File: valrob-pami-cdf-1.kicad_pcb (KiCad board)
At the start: 4 copper layers, 58 x 50 mm, 138 parts, among them J1 Conn_01x04, J2 USB_C_Receptacle_USB2.0_14P, J3 Conn_01x02, J4 Conn_01x04_Pin, J5 Conn_01x06, M1 Motor_Servo, M2 Stepper_Motor_bipolar, M3 Stepper_Motor_bipolar, Q1 Q_NMOS, Q2 Q_NMOS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

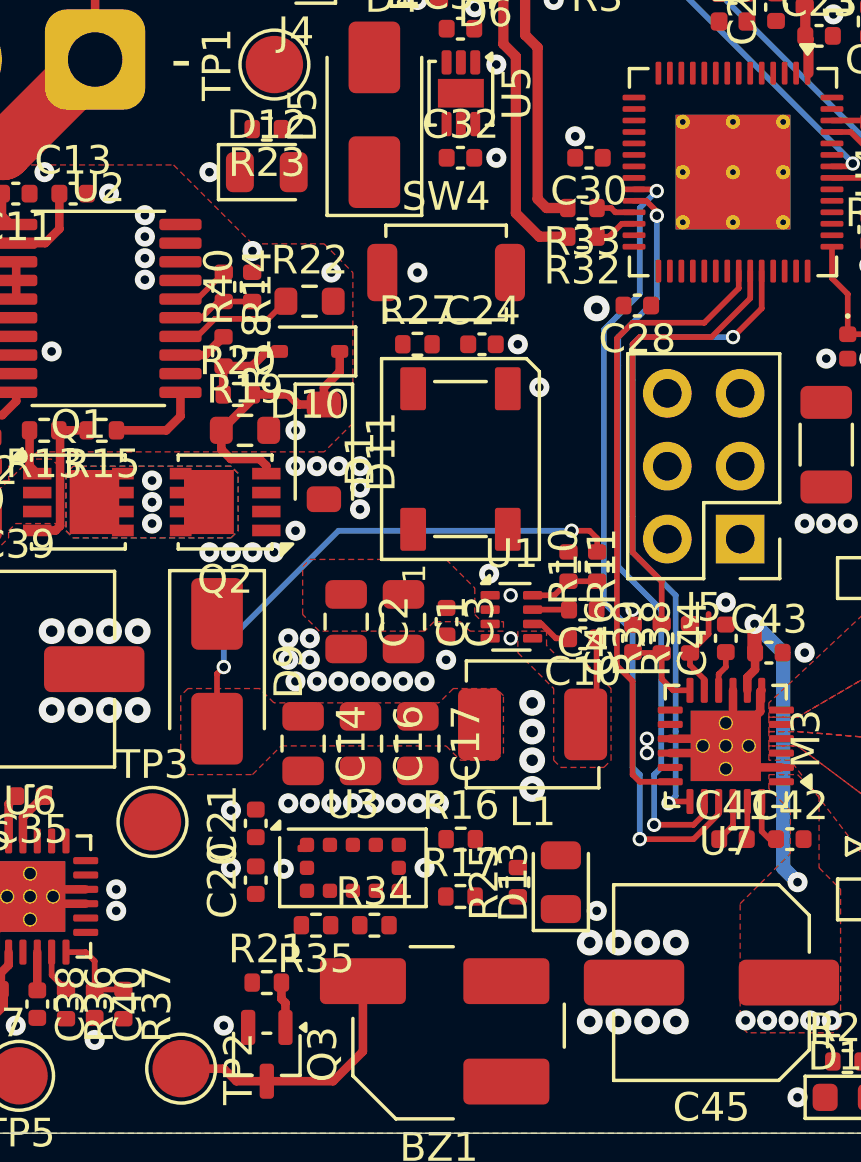
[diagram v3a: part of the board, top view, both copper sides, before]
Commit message: pcb: add buzzer routing
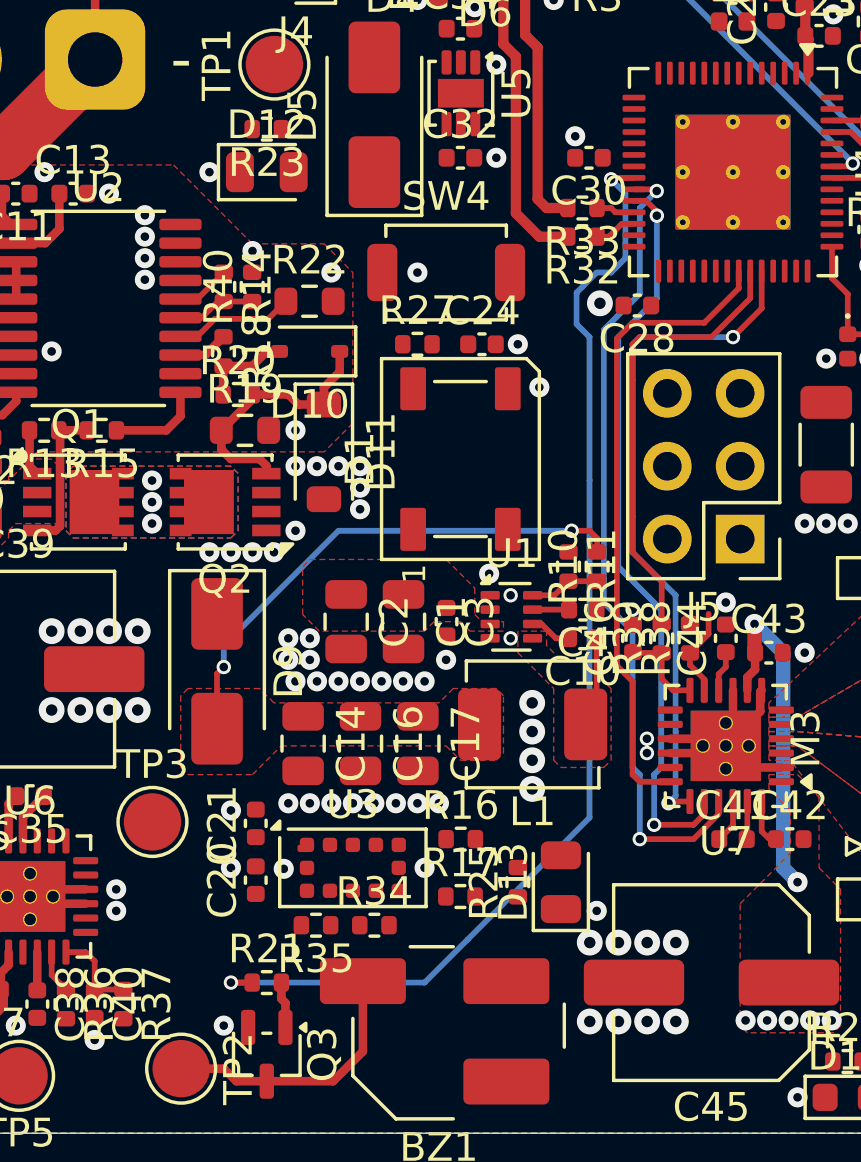
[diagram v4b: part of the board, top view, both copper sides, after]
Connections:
- U4 pad 22: unconnected-(U4-GPIO16/ADC2_CH5/XTAL_32K_N-Pad22) -> /BUZZER
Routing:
- net /BUZZER: track 0.00 -> 40.1 mm, vias 0 -> 2
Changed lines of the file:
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@@
 	(net 110 "unconnected-(U4-SPIQ{slash}GPIO31-Pad34)")
 	(net 111 "/~{SLEEP_2}")
-	(net 112 "unconnected-(U4-GPIO16{slash}ADC2_CH5{slash}XTAL_32K_N-Pad22)")
-	(net 113 "unconnected-(U4-MTDI{slash}JTAG{slash}GPIO41-Pad47)")
-	(net 114 "unconnected-(U6-M1-Pad17)")
-	(net 115 "unconnected-(U6-TOFF-Pad14)")
-	(net 116 "unconnected-(U7-TOFF-Pad14)")
-	(net 117 "unconnected-(U7-M1-Pad17)")
-	(net 118 "unconnected-(D1-DOUT-Pad2)")
-	(net 119 "Net-(J5-Pin_5)")
-	(net 120 "Net-(J5-Pin_4)")
-	(net 121 "Net-(J5-Pin_2)")
-	(net 122 "Net-(J5-Pin_3)")
-	(net 123 "unconnected-(R34-Pad2)")
-	(net 124 "unconnected-(U4-GPIO5{slash}ADC1_CH4-Pad10)")
-	(net 125 "unconnected-(U4-GPIO9{slash}ADC1_CH8-Pad14)")
-	(net 126 "unconnected-(U4-GPIO12{slash}ADC2_CH1-Pad17)")
-	(net 127 "unconnected-(U4-GPIO13{slash}ADC2_CH2-Pad18)")
-	(net 128 "unconnected-(U4-GPIO14{slash}ADC2_CH3-Pad19)")
-	(net 129 "unconnected-(U4-GPIO11{slash}ADC2_CH0-Pad16)")
+	(net 112 "unconnected-(U4-MTDI{slash}JTAG{slash}GPIO41-Pad47)")
+	(net 113 "unconnected-(U6-M1-Pad17)")
+	(net 114 "unconnected-(U6-TOFF-Pad14)")
+	(net 115 "unconnected-(U7-TOFF-Pad14)")
+	(net 116 "unconnected-(U7-M1-Pad17)")
+	(net 117 "unconnected-(D1-DOUT-Pad2)")
+	(net 118 "Net-(J5-Pin_5)")
+	(net 119 "Net-(J5-Pin_4)")
+	(net 120 "Net-(J5-Pin_2)")
+	(net 121 "Net-(J5-Pin_3)")
+	(net 122 "unconnected-(R34-Pad2)")
+	(net 123 "unconnected-(U4-GPIO5{slash}ADC1_CH4-Pad10)")
+	(net 124 "unconnected-(U4-GPIO9{slash}ADC1_CH8-Pad14)")
+	(net 125 "unconnected-(U4-GPIO12{slash}ADC2_CH1-Pad17)")
+	(net 126 "unconnected-(U4-GPIO13{slash}ADC2_CH2-Pad18)")
+	(net 127 "unconnected-(U4-GPIO14{slash}ADC2_CH3-Pad19)")
+	(net 128 "unconnected-(U4-GPIO11{slash}ADC2_CH0-Pad16)")
 	(footprint "GLCS:Texas_RGE0024B_VQFN-24-1EP_4x4mm_P0.5mm_EP2.5x2.5mm_ThermalVias"
 		(layer "F.Cu")
@@
 			(layers "F.Cu" "F.Mask" "F.Paste")
 			(roundrect_rratio 0.25)
-			(net 115 "unconnected-(U6-TOFF-Pad14)")
+			(net 114 "unconnected-(U6-TOFF-Pad14)")
 			(pinfunction "TOFF")
 			(pintype "input+no_connect")
@@
 			(layers "F.Cu" "F.Mask" "F.Paste")
 			(roundrect_rratio 0.25)
-			(net 114 "unconnected-(U6-M1-Pad17)")
+			(net 113 "unconnected-(U6-M1-Pad17)")
 			(pinfunction "M1")
 			(pintype "input+no_connect")
@@
 			(layers "F.Cu" "F.Mask" "F.Paste")
 			(roundrect_rratio 0.1)
-			(net 118 "unconnected-(D1-DOUT-Pad2)")
+			(net 117 "unconnected-(D1-DOUT-Pad2)")
 			(pinfunction "DOUT")
 			(pintype "output+no_connect")
@@
 			(layers "F.Cu" "F.Mask" "F.Paste")
 			(roundrect_rratio 0.25)
-			(net 116 "unconnected-(U7-TOFF-Pad14)")
+			(net 115 "unconnected-(U7-TOFF-Pad14)")
 			(pinfunction "TOFF")
 			(pintype "input+no_connect")
@@
 			(layers "F.Cu" "F.Mask" "F.Paste")
 			(roundrect_rratio 0.25)
-			(net 117 "unconnected-(U7-M1-Pad17)")
+			(net 116 "unconnected-(U7-M1-Pad17)")
 			(pinfunction "M1")
 			(pintype "input+no_connect")
@@
 			(layers "F.Cu" "F.Mask" "F.Paste")
 			(roundrect_rratio 0.25)
-			(net 124 "unconnected-(U4-GPIO5{slash}ADC1_CH4-Pad10)")
+			(net 123 "unconnected-(U4-GPIO5{slash}ADC1_CH4-Pad10)")
 			(pinfunction "GPIO5/ADC1_CH4")
 			(pintype "bidirectional")
@@
 			(layers "F.Cu" "F.Mask" "F.Paste")
 			(roundrect_rratio 0.25)
-			(net 125 "unconnected-(U4-GPIO9{slash}ADC1_CH8-Pad14)")
+			(net 124 "unconnected-(U4-GPIO9{slash}ADC1_CH8-Pad14)")
 			(pinfunction "GPIO9/ADC1_CH8")
 			(pintype "bidirectional")
@@
 			(layers "F.Cu" "F.Mask" "F.Paste")
 			(roundrect_rratio 0.25)
-			(net 129 "unconnected-(U4-GPIO11{slash}ADC2_CH0-Pad16)")
+			(net 128 "unconnected-(U4-GPIO11{slash}ADC2_CH0-Pad16)")
 			(pinfunction "GPIO11/ADC2_CH0")
 			(pintype "bidirectional")
@@
 			(layers "F.Cu" "F.Mask" "F.Paste")
 			(roundrect_rratio 0.25)
-			(net 126 "unconnected-(U4-GPIO12{slash}ADC2_CH1-Pad17)")
+			(net 125 "unconnected-(U4-GPIO12{slash}ADC2_CH1-Pad17)")
 			(pinfunction "GPIO12/ADC2_CH1")
 			(pintype "bidirectional")
@@
 			(layers "F.Cu" "F.Mask" "F.Paste")
 			(roundrect_rratio 0.25)
-			(net 127 "unconnected-(U4-GPIO13{slash}ADC2_CH2-Pad18)")
+			(net 126 "unconnected-(U4-GPIO13{slash}ADC2_CH2-Pad18)")
 			(pinfunction "GPIO13/ADC2_CH2")
 			(pintype "bidirectional")
@@
 			(layers "F.Cu" "F.Mask" "F.Paste")
 			(roundrect_rratio 0.25)
-			(net 128 "unconnected-(U4-GPIO14{slash}ADC2_CH3-Pad19)")
+			(net 127 "unconnected-(U4-GPIO14{slash}ADC2_CH3-Pad19)")
 			(pinfunction "GPIO14/ADC2_CH3")
 			(pintype "bidirectional")
@@
 			(layers "F.Cu" "F.Mask" "F.Paste")
 			(roundrect_rratio 0.25)
-			(net 112 "unconnected-(U4-GPIO16{slash}ADC2_CH5{slash}XTAL_32K_N-Pad22)")
+			(net 75 "/BUZZER")
 			(pinfunction "GPIO16/ADC2_CH5/XTAL_32K_N")
-			(pintype "bidirectional+no_connect")
+			(pintype "bidirectional")
 		)
 		(pad "23" smd roundrect
@@
 			(layers "F.Cu" "F.Mask" "F.Paste")
 			(roundrect_rratio 0.25)
-			(net 121 "Net-(J5-Pin_2)")
+			(net 120 "Net-(J5-Pin_2)")
 			(pinfunction "GPIO34")
 			(pintype "bidirectional")
@@
 			(layers "F.Cu" "F.Mask" "F.Paste")
 			(roundrect_rratio 0.25)
-			(net 122 "Net-(J5-Pin_3)")
+			(net 121 "Net-(J5-Pin_3)")
 			(pinfunction "GPIO35")
 			(pintype "bidirectional")
@@
 			(layers "F.Cu" "F.Mask" "F.Paste")
 			(roundrect_rratio 0.25)
-			(net 120 "Net-(J5-Pin_4)")
+			(net 119 "Net-(J5-Pin_4)")
 			(pinfunction "GPIO36")
 			(pintype "bidirectional")
@@
 			(layers "F.Cu" "F.Mask" "F.Paste")
 			(roundrect_rratio 0.25)
-			(net 119 "Net-(J5-Pin_5)")
+			(net 118 "Net-(J5-Pin_5)")
 			(pinfunction "GPIO37")
 			(pintype "bidirectional")
@@
 			(layers "F.Cu" "F.Mask" "F.Paste")
 			(roundrect_rratio 0.25)
-			(net 113 "unconnected-(U4-MTDI{slash}JTAG{slash}GPIO41-Pad47)")
+			(net 112 "unconnected-(U4-MTDI{slash}JTAG{slash}GPIO41-Pad47)")
 			(pinfunction "MTDI/JTAG/GPIO41")
 			(pintype "bidirectional+no_connect")
@@
 			(layers "F.Cu" "F.Mask" "F.Paste")
 			(roundrect_rratio 0.25)
-			(net 123 "unconnected-(R34-Pad2)")
+			(net 122 "unconnected-(R34-Pad2)")
 			(pintype "passive")
 		)
@@
 			(layers "*.Cu" "*.Mask")
 			(remove_unused_layers no)
-			(net 121 "Net-(J5-Pin_2)")
+			(net 120 "Net-(J5-Pin_2)")
 			(pinfunction "Pin_2")
 			(pintype "passive")
@@
 			(layers "*.Cu" "*.Mask")
 			(remove_unused_layers no)
-			(net 122 "Net-(J5-Pin_3)")
+			(net 121 "Net-(J5-Pin_3)")
 			(pinfunction "Pin_3")
 			(pintype "passive")
@@
 			(layers "*.Cu" "*.Mask")
 			(remove_unused_layers no)
-			(net 120 "Net-(J5-Pin_4)")
+			(net 119 "Net-(J5-Pin_4)")
 			(pinfunction "Pin_4")
 			(pintype "passive")
@@
 			(layers "*.Cu" "*.Mask")
 			(remove_unused_layers no)
-			(net 119 "Net-(J5-Pin_5)")
+			(net 118 "Net-(J5-Pin_5)")
 			(pinfunction "Pin_5")
 			(pintype "passive")
@@
 	)
 	(via
-		(at 164 94.25)
+		(at 164.111979 94.071793)
 		(size 0.9)
 		(drill 0.4)
@@
 	)
 	(segment
+		(start 165.3 89.7)
+		(end 164.55 89.7)
+		(width 0.2)
+		(layer "F.Cu")
+		(net 75)
+	)
+	(segment
+		(start 151.99 117.75)
+		(end 151.25 117.75)
+		(width 0.2)
+		(layer "F.Cu")
+		(net 75)
+	)
+	(segment
+		(start 164.55 89.7)
+		(end 164.5 89.75)
+		(width 0.2)
+		(layer "F.Cu")
+		(net 75)
+	)
+	(via
+		(at 151.25 117.75)
+		(size 0.5)
+		(drill 0.3)
+		(layers "F.Cu" "B.Cu")
+		(net 75)
+	)
+	(via
+		(at 164.5 89.75)
+		(size 0.5)
+		(drill 0.3)
+		(layers "F.Cu" "B.Cu")
+		(net 75)
+	)
+	(segment
+		(start 165 92.5)
+		(end 165 92)
+		(width 0.2)
+		(layer "B.Cu")
+		(net 75)
+	)
+	(segment
+		(start 164 93)
+		(end 164.5 93)
+		(width 0.2)
+		(layer "B.Cu")
+		(net 75)
+	)
+	(segment
+		(start 163.75 95.25)
+		(end 163.5 95)
+		(width 0.2)
+		(layer "B.Cu")
+		(net 75)
+	)
+	(segment
+		(start 163.5 93.5)
+		(end 164 93)
+		(width 0.2)
+		(layer "B.Cu")
+		(net 75)
+	)
+	(segment
+		(start 163.299 94.799)
+		(end 163.299 93.701)
+		(width 0.2)
+		(layer "B.Cu")
+		(net 75)
+	)
+	(segment
+		(start 164.5 93)
+		(end 165 92.5)
+		(width 0.2)
+		(layer "B.Cu")
+		(net 75)
+	)
+	(segment
+		(start 158 117.75)
+		(end 159.5 116.25)
+		(width 0.2)
+		(layer "B.Cu")
+		(net 75)
+	)
+	(segment
+		(start 159.5 116.25)
+		(end 163.75 112)
+		(width 0.2)
+		(layer "B.Cu")
+		(net 75)
+	)
+	(segment
+		(start 163.299 93.701)
+		(end 163.5 93.5)
+		(width 0.2)
+		(layer "B.Cu")
+		(net 75)
+	)
+	(segment
+		(start 163.75 100.25)
+		(end 163.75 95.25)
+		(width 0.2)
+		(layer "B.Cu")
+		(net 75)
+	)
+	(segment
+		(start 163.5 95)
+		(end 163.299 94.799)
+		(width 0.2)
+		(layer "B.Cu")
+		(net 75)
+	)
+	(segment
+		(start 165 92)
+		(end 165 90.25)
+		(width 0.2)
+		(layer "B.Cu")
+		(net 75)
+	)
+	(segment
+		(start 151.25 117.75)
+		(end 158 117.75)
+		(width 0.2)
+		(layer "B.Cu")
+		(net 75)
+	)
+	(segment
+		(start 163.75 112)
+		(end 163.75 100.25)
+		(width 0.2)
+		(layer "B.Cu")
+		(net 75)
+	)
+	(segment
+		(start 165 90.25)
+		(end 164.5 89.75)
+		(width 0.2)
+		(layer "B.Cu")
+		(net 75)
+	)
+	(segment

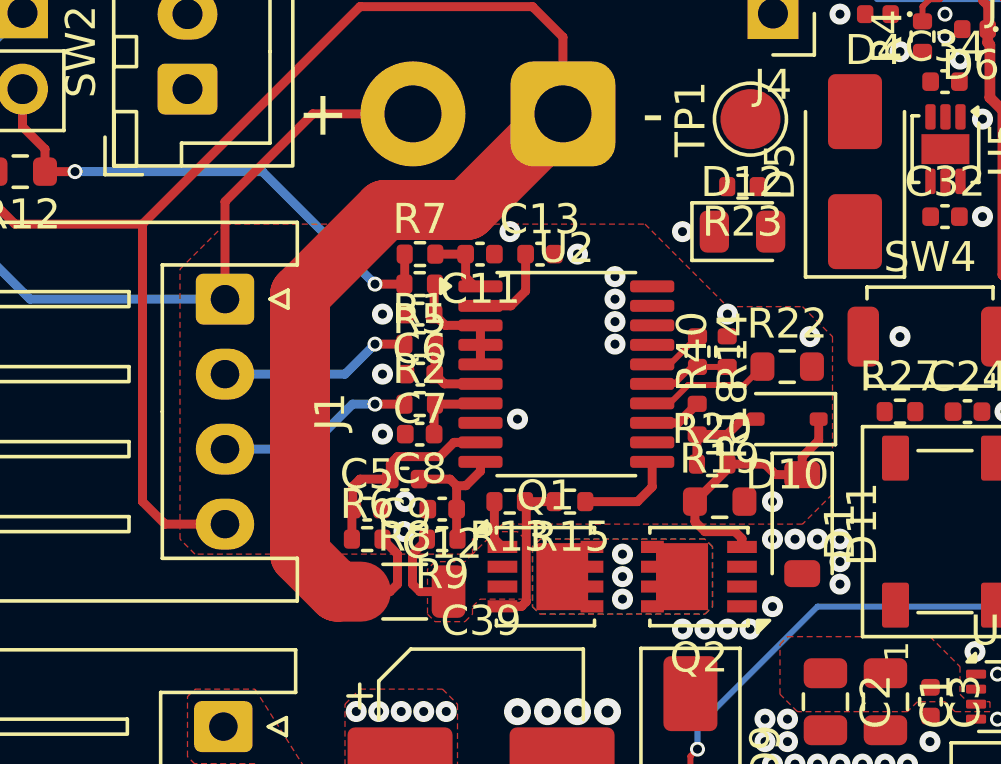
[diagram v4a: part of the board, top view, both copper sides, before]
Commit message: pcb: fix bms BGND pour
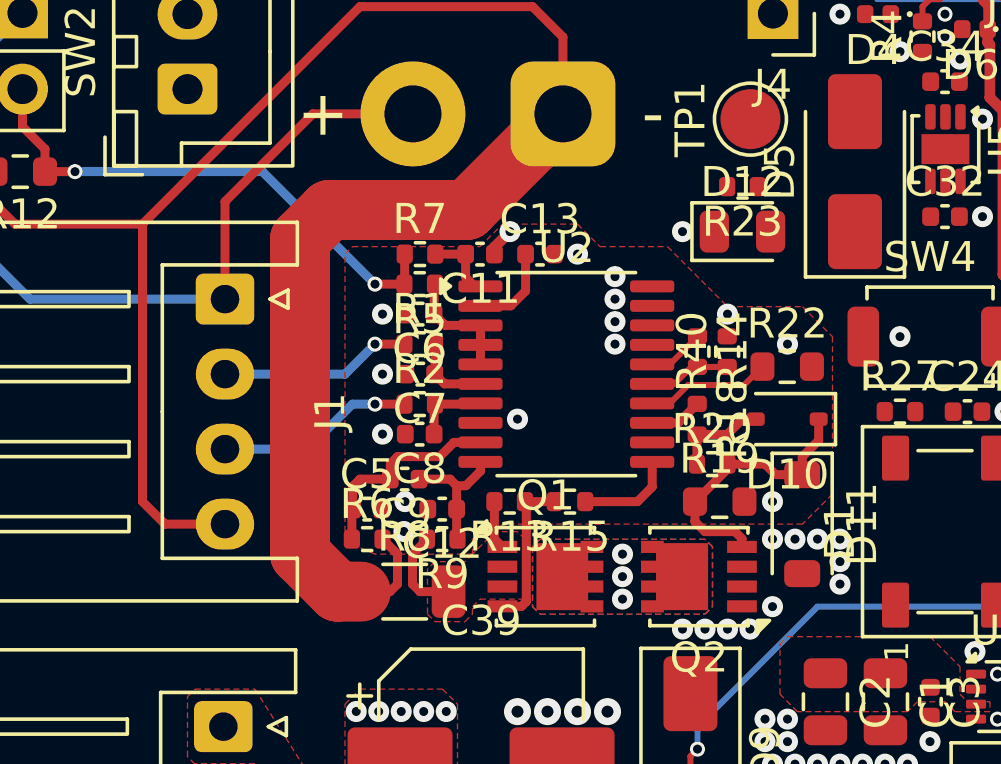
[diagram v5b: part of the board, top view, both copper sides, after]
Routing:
- net BGND: track 64.1 -> 72.4 mm
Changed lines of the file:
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@@
 	)
 	(via
-		(at 154.75 93)
+		(at 154 93.25)
 		(size 0.7)
 		(drill 0.3)
@@
 	)
 	(segment
+		(start 146.515 85.575)
+		(end 143.311 88.779)
+		(width 2)
+		(layer "F.Cu")
+		(net 7)
+	)
+	(segment
 		(start 128.25 89.25)
 		(end 127.6 88.6)
@@
 	)
 	(segment
-		(start 139 101.5)
-		(end 139.7775 101.5)
+		(start 137.75 89.75)
+		(end 137.75 100.25)
 		(width 2)
 		(layer "F.Cu")
@@
 	)
 	(segment
-		(start 143.311 88.779)
-		(end 140.56858 88.779)
-		(width 2)
+		(start 140.75 101.5)
+		(end 139.7775 101.5)
+		(width 0.3)
 		(layer "F.Cu")
 		(net 7)
 	)
 	(segment
-		(start 140.75 101.5)
+		(start 139 101.5)
 		(end 139.7775 101.5)
-		(width 0.3)
+		(width 2)
 		(layer "F.Cu")
 		(net 7)
@@
 	)
 	(segment
-		(start 140.56858 88.779)
-		(end 137.75 91.59758)
+		(start 137.75 100.25)
+		(end 139 101.5)
+		(width 2)
+		(layer "F.Cu")
+		(net 7)
+	)
+	(segment
+		(start 144.23 90.25)
+		(end 144.23 90.02)
+		(width 0.359)
+		(layer "F.Cu")
+		(net 7)
+	)
+	(segment
+		(start 138.721 88.779)
+		(end 137.75 89.75)
 		(width 2)
 		(layer "F.Cu")
@@
 	)
 	(segment
-		(start 137.75 91.59758)
-		(end 137.75 100.25)
-		(width 2)
+		(start 132.5 89.25)
+		(end 128.25 89.25)
+		(width 0.3)
 		(layer "F.Cu")
 		(net 7)
 	)
 	(segment
-		(start 132.5 89.25)
-		(end 128.25 89.25)
+		(start 132.5 89.75)
+		(end 132.5 89.25)
 		(width 0.3)
 		(layer "F.Cu")
@@
 	)
 	(segment
-		(start 137.75 100.25)
-		(end 139 101.5)
+		(start 143.311 88.779)
+		(end 138.721 88.779)
 		(width 2)
 		(layer "F.Cu")
@@
 	)
 	(segment
-		(start 132.5 89.75)
-		(end 132.5 89.25)
+		(start 145.5 82)
+		(end 146.515 83.015)
 		(width 0.3)
 		(layer "F.Cu")
@@
 	)
 	(segment
-		(start 145.5 82)
-		(end 146.515 83.015)
-		(width 0.3)
+		(start 144.23 90.02)
+		(end 144.75 89.5)
+		(width 0.359)
 		(layer "F.Cu")
 		(net 7)
@@
 	)
 	(segment
-		(start 146.515 85.575)
-		(end 143.311 88.779)
-		(width 2)
-		(layer "F.Cu")
-		(net 7)
-	)
-	(segment
 		(start 135.25 99.25)
 		(end 133.25 99.25)
@@
 	)
 	(segment
+		(start 140.5 99.25)
+		(end 141.25 98.5)
+		(width 2)
+		(layer "In1.Cu")
+		(net 7)
+	)
+	(segment
+		(start 135.25 99.25)
+		(end 140.5 99.25)
+		(width 2)
+		(layer "In1.Cu")
+		(net 7)
+	)
+	(segment
 		(start 142.40755 97)
 		(end 141 97)
@@
 		(polygon
 			(pts
-				(xy 134.25 100.25) (xy 133.75 99.75) (xy 133.75 90.75) (xy 135.25 89.25) (xy 149.25 89.25) (xy 152 92)
-				(xy 154.5 92) (xy 155.5 93) (xy 155.5 98.25) (xy 154.5 99.25) (xy 144.5 99.25) (xy 143.5 100.25)
+				(xy 140.25 100.25) (xy 139.25 99.821429) (xy 139.25 90.25) (xy 139.5 90) (xy 143.75 90) (xy 144.5 89.25)
+				(xy 147 89.25) (xy 147.75 90) (xy 150 90) (xy 152 92) (xy 154.5 92) (xy 155.5 93) (xy 155.5 98.25)
+				(xy 154.5 99.25) (xy 144.5 99.25) (xy 143.5 100.25)
 			)
 		)
